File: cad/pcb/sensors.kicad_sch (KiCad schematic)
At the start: 7 parts, among them IC4 MXC4005XC, IC5 KTS1620ERG-TR, Q2 1541201NEA400

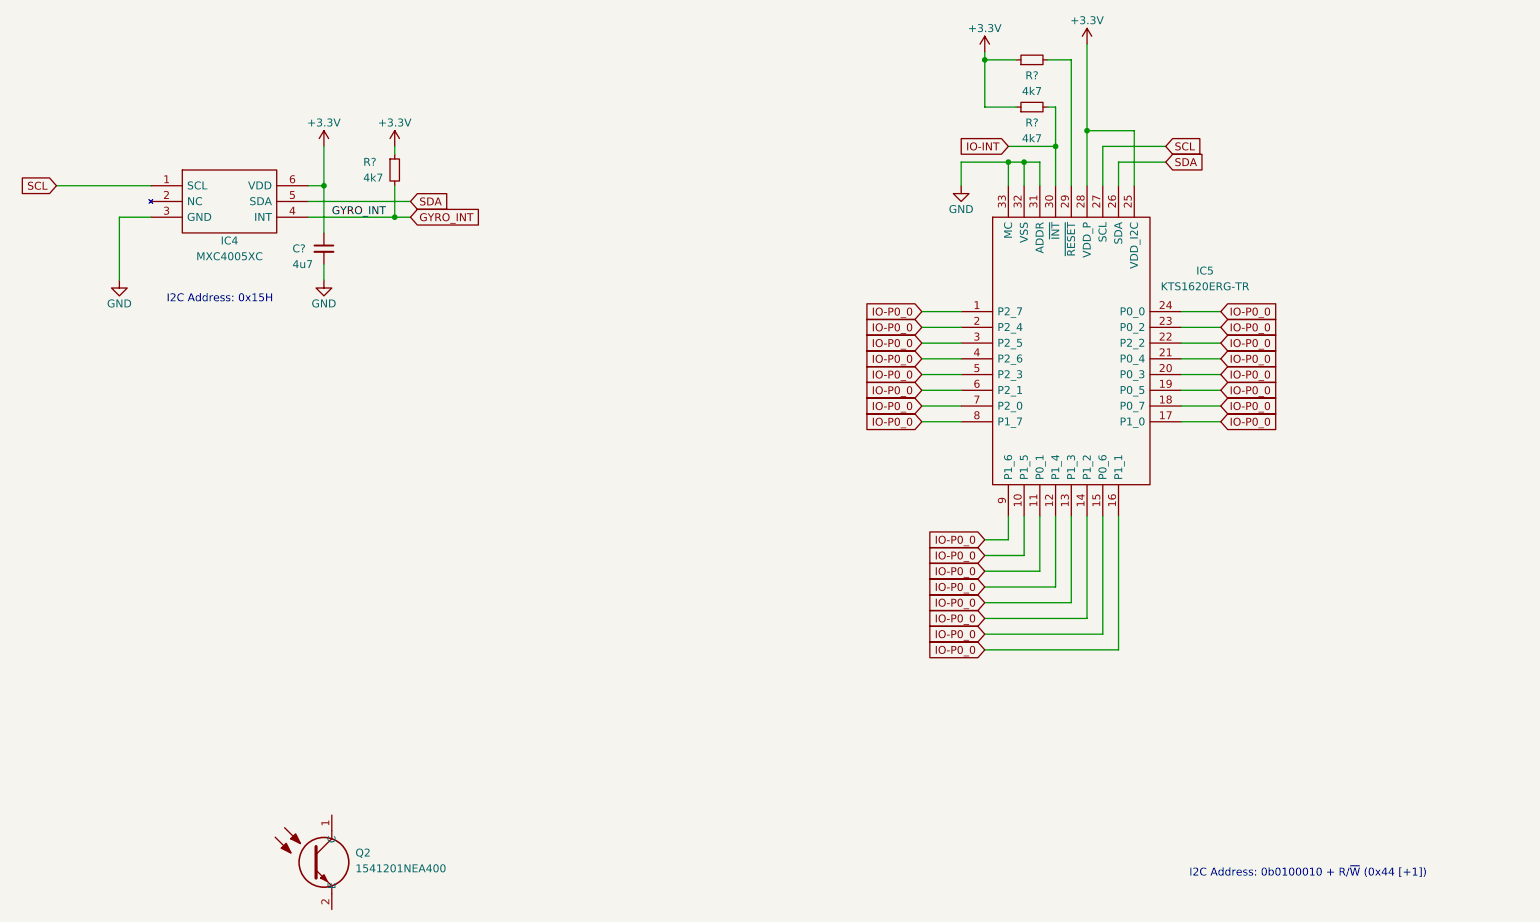
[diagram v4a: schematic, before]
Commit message: add LEDs for LED ring
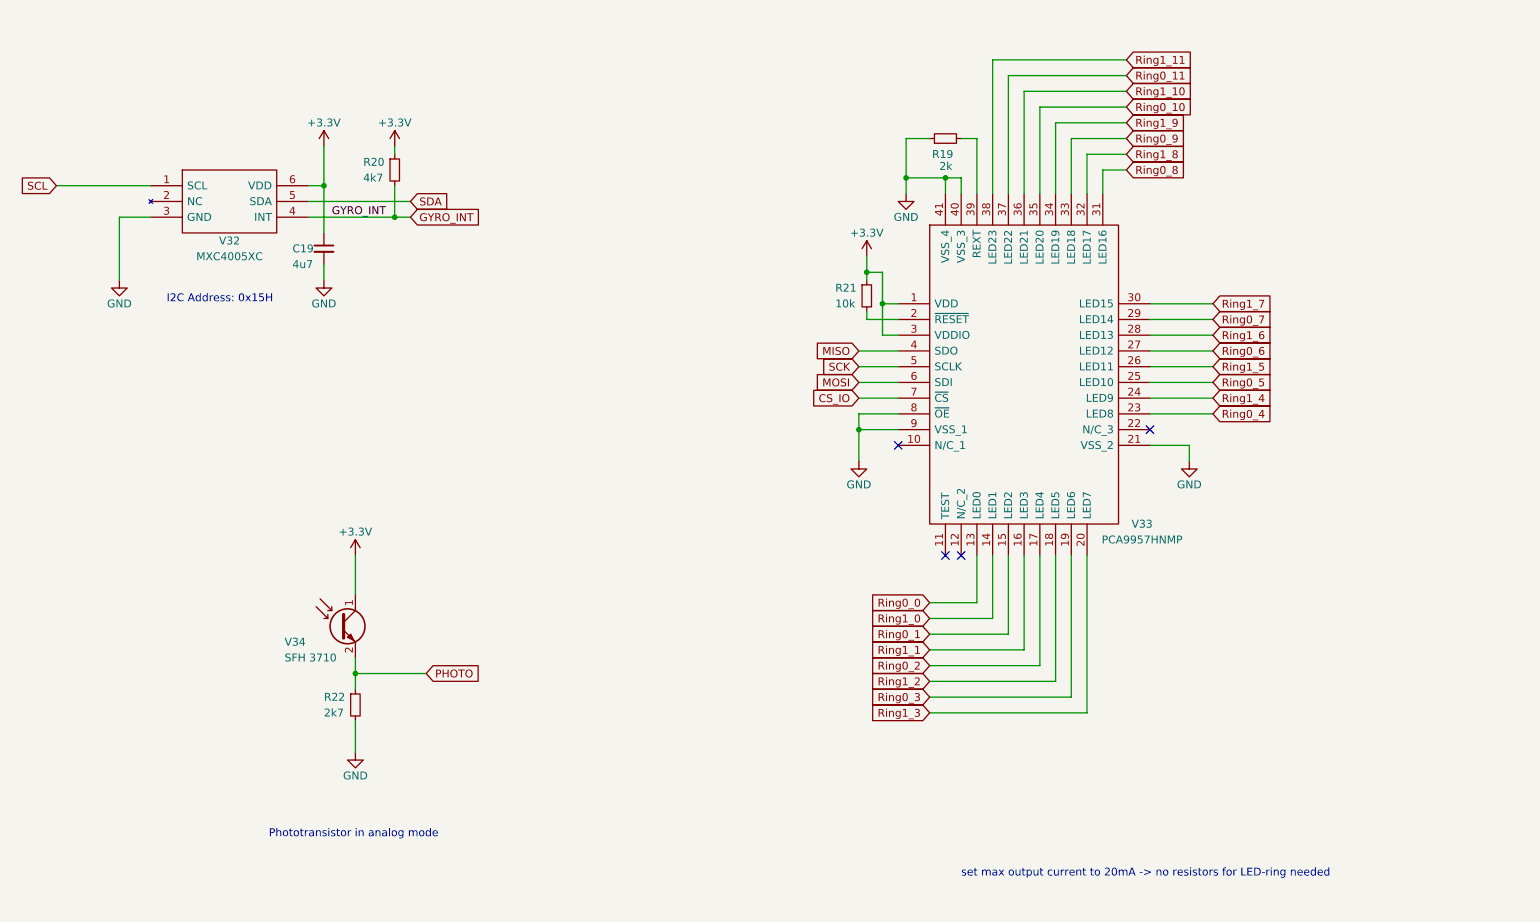
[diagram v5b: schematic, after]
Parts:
- removed IC5: KTS1620ERG-TR, QFN50P500X500X80-33N-D, symbol I/O-Expander:KTS1620ERG-TR
- removed Q2: 1541201NEA400, 1541201NEA400, symbol Phototransistor:1541201NEA400
- removed R? (x2): 4k7, symbol Device:R_Small
- added R19: 2k, symbol Device:R_Small
- added R21: 10k, symbol Device:R_Small
- added R22: 2k7, symbol Device:R_Small
- added V33: PCA9957HNMP, IO Expander:PCA9957HNMP, symbol I/O-Expander:PCA9957HNMP
- added V34: SFH 3710, symbol Device:Q_Photo_NPN
- V32: renamed from IC4; footprint MXC4005XC -> Gyroscope:MXC4005XC
- gave numbers to parts that had none: 2
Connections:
- net +3.3V: now also R21.1, V33.1 (VDD), V33.3 (VDDIO), V34.1 (C)
- net GND: now also R19.1, R22.2, V33.21 (VSS_2), V33.40 (VSS_3), V33.41 (VSS_4), V33.8 (~{OE}), V33.9 (VSS_1)
- new net: R21.2, V33.2 (~{RESET})
- new net: R19.2, V33.39 (REXT)
- new net CS_IO: V33.7 (~{CS})
- new net MISO: V33.4 (SDO)
- new net MOSI: V33.6 (SDI)
- new net PHOTO: R22.1, V34.2 (E)
- new net Ring0_0: V33.13 (LED0)
- new net Ring0_1: V33.15 (LED2)
- new net Ring0_10: V33.35 (LED20)
- new net Ring0_11: V33.37 (LED22)
- new net Ring0_2: V33.17 (LED4)
- new net Ring0_3: V33.19 (LED6)
- new net Ring0_4: V33.23 (LED8)
- new net Ring0_5: V33.25 (LED10)
- new net Ring0_6: V33.27 (LED12)
- new net Ring0_7: V33.29 (LED14)
- new net Ring0_8: V33.31 (LED16)
- new net Ring0_9: V33.33 (LED18)
- new net Ring1_0: V33.14 (LED1)
- new net Ring1_1: V33.16 (LED3)
- new net Ring1_10: V33.36 (LED21)
- new net Ring1_11: V33.38 (LED23)
- new net Ring1_2: V33.18 (LED5)
- new net Ring1_3: V33.20 (LED7)
- new net Ring1_4: V33.24 (LED9)
- new net Ring1_5: V33.26 (LED11)
- new net Ring1_6: V33.28 (LED13)
- new net Ring1_7: V33.30 (LED15)
- new net Ring1_8: V33.32 (LED17)
- new net Ring1_9: V33.34 (LED19)
- new net SCK: V33.5 (SCLK)
- no-connect marks 0 -> 4
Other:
- note added: "Phototransistor in analog mode"
- note added: "set max output current to 20mA -> no resistors for LED-ring needed"
- note removed: "I2C Address: 0b0100010 + R/~{W} (0x44 [+1])"

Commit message: add testpoints & connectors
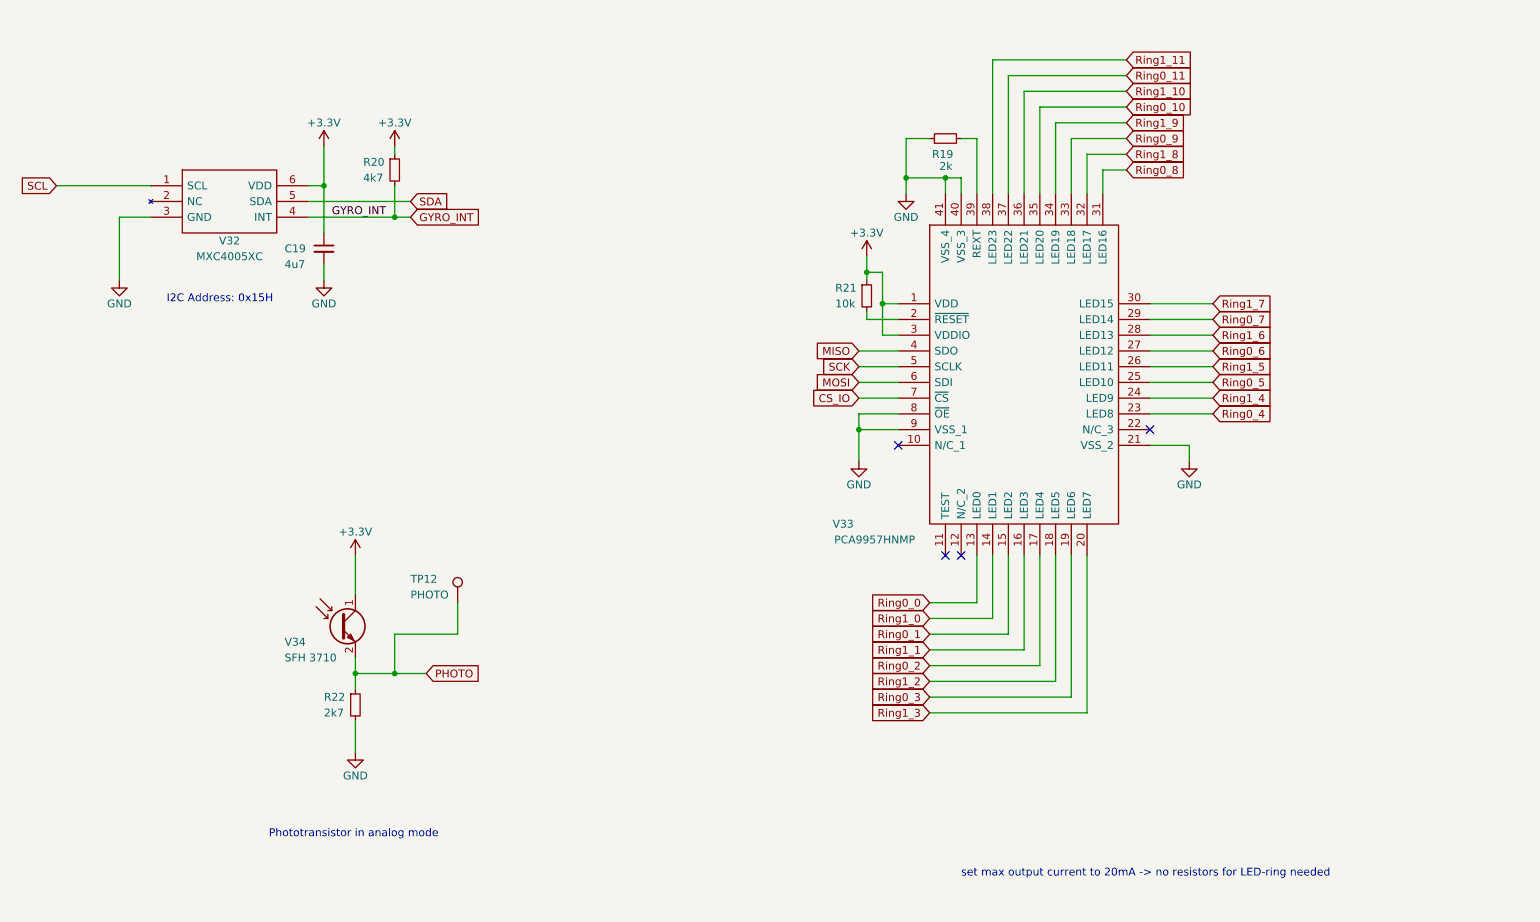
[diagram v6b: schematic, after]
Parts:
- added TP12: PHOTO, symbol Connector:TestPoint
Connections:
- net PHOTO: now also TP12.1
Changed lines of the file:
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@@
   (junction (at 168.91 91.44) (diameter 0) (color 0 0 0 0)
+  )
+  (junction (at 93.98 130.81) (diameter 0) (color 0 0 0 0)
   )
   (junction (at 93.98 57.15) (diameter 0) (color 0 0 0 0)
@@
     (stroke (width 0) (type default) (color 0 0 0 0))
   )
-  (wire (pts (xy 99.06 130.81) (xy 87.63 130.81))
+  (wire (pts (xy 99.06 130.81) (xy 93.98 130.81))
     (stroke (width 0) (type default) (color 0 0 0 0))
   )
@@
     (stroke (width 0) (type default) (color 0 0 0 0))
   )
+  (wire (pts (xy 93.98 124.46) (xy 93.98 130.81))
+    (stroke (width 0) (type default) (color 0 0 0 0))
+  )
   (wire (pts (xy 200.66 111.76) (xy 200.66 132.08))
     (stroke (width 0) (type default) (color 0 0 0 0))
@@
     (stroke (width 0) (type default) (color 0 0 0 0))
   )
+  (wire (pts (xy 104.14 119.38) (xy 104.14 124.46))
+    (stroke (width 0) (type default) (color 0 0 0 0))
+  )
   (wire (pts (xy 80.01 54.61) (xy 96.52 54.61))
     (stroke (width 0) (type default) (color 0 0 0 0))
@@
     (stroke (width 0) (type default) (color 0 0 0 0))
   )
+  (wire (pts (xy 93.98 130.81) (xy 87.63 130.81))
+    (stroke (width 0) (type default) (color 0 0 0 0))
+  )
   (wire (pts (xy 215.9 71.12) (xy 226.06 71.12))
     (stroke (width 0) (type default) (color 0 0 0 0))
@@
   )
   (wire (pts (xy 87.63 143.51) (xy 87.63 138.43))
+    (stroke (width 0) (type default) (color 0 0 0 0))
+  )
+  (wire (pts (xy 104.14 124.46) (xy 93.98 124.46))
     (stroke (width 0) (type default) (color 0 0 0 0))
   )
@@
   (symbol (lib_id "power:+3.3V") (at 82.55 45.72 0) (unit 1)
     (in_bom yes) (on_board yes)
-    (property "Reference" "#PWR063" (id 0) (at 82.55 49.53 0)
+    (property "Reference" "#PWR066" (id 0) (at 82.55 49.53 0)
       (effects (font (size 1.27 1.27)) hide)
     )
@@
   (symbol (lib_id "power:GND") (at 49.53 67.31 0) (unit 1)
     (in_bom yes) (on_board yes)
-    (property "Reference" "#PWR067" (id 0) (at 49.53 73.66 0)
+    (property "Reference" "#PWR070" (id 0) (at 49.53 73.66 0)
       (effects (font (size 1.27 1.27)) hide)
     )
@@
   (symbol (lib_id "power:+3.3V") (at 170.18 63.5 0) (unit 1)
     (in_bom yes) (on_board yes)
-    (property "Reference" "#PWR066" (id 0) (at 170.18 67.31 0)
+    (property "Reference" "#PWR069" (id 0) (at 170.18 67.31 0)
       (effects (font (size 1.27 1.27)) hide)
     )
@@
   (symbol (lib_id "power:GND") (at 87.63 143.51 0) (unit 1)
     (in_bom yes) (on_board yes)
-    (property "Reference" "#PWR072" (id 0) (at 87.63 149.86 0)
+    (property "Reference" "#PWR075" (id 0) (at 87.63 149.86 0)
       (effects (font (size 1.27 1.27)) hide)
     )
@@
   (symbol (lib_id "power:GND") (at 176.53 53.34 0) (unit 1)
     (in_bom yes) (on_board yes)
-    (property "Reference" "#PWR065" (id 0) (at 176.53 59.69 0)
+    (property "Reference" "#PWR068" (id 0) (at 176.53 59.69 0)
       (effects (font (size 1.27 1.27)) hide)
     )
@@
   (symbol (lib_id "power:GND") (at 82.55 67.31 0) (unit 1)
     (in_bom yes) (on_board yes)
-    (property "Reference" "#PWR068" (id 0) (at 82.55 73.66 0)
+    (property "Reference" "#PWR071" (id 0) (at 82.55 73.66 0)
       (effects (font (size 1.27 1.27)) hide)
     )
@@
   (symbol (lib_id "power:GND") (at 168.91 96.52 0) (unit 1)
     (in_bom yes) (on_board yes)
-    (property "Reference" "#PWR069" (id 0) (at 168.91 102.87 0)
+    (property "Reference" "#PWR072" (id 0) (at 168.91 102.87 0)
       (effects (font (size 1.27 1.27)) hide)
     )
@@
   (symbol (lib_id "Device:C_Small") (at 82.55 62.23 0) (unit 1)
     (in_bom yes) (on_board yes)
-    (property "Reference" "C19" (id 0) (at 77.47 62.23 0)
-      (effects (font (size 1.27 1.27)) (justify left))
-    )
-    (property "Value" "4u7" (id 1) (at 77.47 64.77 0)
+    (property "Reference" "C19" (id 0) (at 76.2 62.23 0)
+      (effects (font (size 1.27 1.27)) (justify left))
+    )
+    (property "Value" "4u7" (id 1) (at 76.2 64.77 0)
       (effects (font (size 1.27 1.27)) (justify left))
     )
@@
   (symbol (lib_id "I{slash}O-Expander:PCA9957HNMP") (at 175.26 71.12 0) (unit 1)
     (in_bom yes) (on_board yes)
-    (property "Reference" "V33" (id 0) (at 214.63 106.68 0))
-    (property "Value" "PCA9957HNMP" (id 1) (at 214.63 109.22 0))
+    (property "Reference" "V33" (id 0) (at 166.37 106.68 0))
+    (property "Value" "PCA9957HNMP" (id 1) (at 171.45 109.22 0))
     (property "Footprint" "IO Expander:PCA9957HNMP" (id 2) (at 212.09 58.42 0)
       (effects (font (size 1.27 1.27)) (justify left) hide)
@@
   (symbol (lib_id "power:GND") (at 222.25 96.52 0) (unit 1)
     (in_bom yes) (on_board yes)
-    (property "Reference" "#PWR070" (id 0) (at 222.25 102.87 0)
+    (property "Reference" "#PWR073" (id 0) (at 222.25 102.87 0)
       (effects (font (size 1.27 1.27)) hide)
     )
@@
     (pin "1")
   )
+  (symbol (lib_id "Connector:TestPoint") (at 104.14 119.38 0) (unit 1)
+    (in_bom yes) (on_board yes)
+    (property "Reference" "TP12" (id 0) (at 96.52 115.57 0)
+      (effects (font (size 1.27 1.27)) (justify left))
+    )
+    (property "Value" "PHOTO" (id 1) (at 96.52 118.11 0)
+      (effects (font (size 1.27 1.27)) (justify left))
+    )
+    (property "Footprint" "" (id 2) (at 109.22 119.38 0)
+      (effects (font (size 1.27 1.27)) hide)
+    )
+    (property "Datasheet" "~" (id 3) (at 109.22 119.38 0)
+      (effects (font (size 1.27 1.27)) hide)
+    )
+    (pin "1")
+  )
   (symbol (lib_id "power:+3.3V") (at 93.98 45.72 0) (unit 1)
     (in_bom yes) (on_board yes)
-    (property "Reference" "#PWR064" (id 0) (at 93.98 49.53 0)
+    (property "Reference" "#PWR067" (id 0) (at 93.98 49.53 0)
       (effects (font (size 1.27 1.27)) hide)
     )
@@
   (symbol (lib_id "power:+3.3V") (at 87.63 111.76 0) (unit 1)
     (in_bom yes) (on_board yes)
-    (property "Reference" "#PWR071" (id 0) (at 87.63 115.57 0)
-      (effects (font (size 1.27 1.27)) hide)
-    )
+    (property "Reference" "#PWR074" (id 0) (at 87.63 115.57 0)
+      (effects (font (size 1.27 1.27)) hide)
+    )

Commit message: add usb-c footprint
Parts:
- renumbered R19 to R22, R20 to R23, R21 to R24, R22 to R25
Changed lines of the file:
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@@
   (symbol (lib_id "power:+3.3V") (at 82.55 45.72 0) (unit 1)
     (in_bom yes) (on_board yes)
-    (property "Reference" "#PWR066" (id 0) (at 82.55 49.53 0)
+    (property "Reference" "#PWR072" (id 0) (at 82.55 49.53 0)
       (effects (font (size 1.27 1.27)) hide)
     )
@@
   (symbol (lib_id "power:GND") (at 49.53 67.31 0) (unit 1)
     (in_bom yes) (on_board yes)
-    (property "Reference" "#PWR070" (id 0) (at 49.53 73.66 0)
+    (property "Reference" "#PWR076" (id 0) (at 49.53 73.66 0)
       (effects (font (size 1.27 1.27)) hide)
     )
@@
   (symbol (lib_id "Device:R_Small") (at 170.18 69.85 0) (unit 1)
     (in_bom yes) (on_board yes)
-    (property "Reference" "R21" (id 0) (at 165.1 68.58 0)
+    (property "Reference" "R24" (id 0) (at 165.1 68.58 0)
       (effects (font (size 1.27 1.27)) (justify left))
     )
@@
   (symbol (lib_id "power:+3.3V") (at 170.18 63.5 0) (unit 1)
     (in_bom yes) (on_board yes)
-    (property "Reference" "#PWR069" (id 0) (at 170.18 67.31 0)
+    (property "Reference" "#PWR075" (id 0) (at 170.18 67.31 0)
       (effects (font (size 1.27 1.27)) hide)
     )
@@
   (symbol (lib_id "power:GND") (at 87.63 143.51 0) (unit 1)
     (in_bom yes) (on_board yes)
-    (property "Reference" "#PWR075" (id 0) (at 87.63 149.86 0)
+    (property "Reference" "#PWR081" (id 0) (at 87.63 149.86 0)
       (effects (font (size 1.27 1.27)) hide)
     )
@@
   (symbol (lib_id "Device:R_Small") (at 93.98 49.53 0) (unit 1)
     (in_bom yes) (on_board yes)
-    (property "Reference" "R20" (id 0) (at 88.9 48.26 0)
+    (property "Reference" "R23" (id 0) (at 88.9 48.26 0)
       (effects (font (size 1.27 1.27)) (justify left))
     )
@@
   (symbol (lib_id "Device:R_Small") (at 182.88 44.45 90) (unit 1)
     (in_bom yes) (on_board yes)
-    (property "Reference" "R19" (id 0) (at 184.15 46.99 90)
+    (property "Reference" "R22" (id 0) (at 184.15 46.99 90)
       (effects (font (size 1.27 1.27)) (justify left))
     )
@@
   (symbol (lib_id "power:GND") (at 176.53 53.34 0) (unit 1)
     (in_bom yes) (on_board yes)
-    (property "Reference" "#PWR068" (id 0) (at 176.53 59.69 0)
+    (property "Reference" "#PWR074" (id 0) (at 176.53 59.69 0)
       (effects (font (size 1.27 1.27)) hide)
     )
@@
   (symbol (lib_id "power:GND") (at 82.55 67.31 0) (unit 1)
     (in_bom yes) (on_board yes)
-    (property "Reference" "#PWR071" (id 0) (at 82.55 73.66 0)
+    (property "Reference" "#PWR077" (id 0) (at 82.55 73.66 0)
       (effects (font (size 1.27 1.27)) hide)
     )
@@
   (symbol (lib_id "power:GND") (at 168.91 96.52 0) (unit 1)
     (in_bom yes) (on_board yes)
-    (property "Reference" "#PWR072" (id 0) (at 168.91 102.87 0)
+    (property "Reference" "#PWR078" (id 0) (at 168.91 102.87 0)
       (effects (font (size 1.27 1.27)) hide)
     )
@@
   (symbol (lib_id "Device:R_Small") (at 87.63 135.89 0) (unit 1)
     (in_bom yes) (on_board yes)
-    (property "Reference" "R22" (id 0) (at 82.55 134.62 0)
+    (property "Reference" "R25" (id 0) (at 82.55 134.62 0)
       (effects (font (size 1.27 1.27)) (justify left))
     )
@@
   (symbol (lib_id "power:GND") (at 222.25 96.52 0) (unit 1)
     (in_bom yes) (on_board yes)
-    (property "Reference" "#PWR073" (id 0) (at 222.25 102.87 0)
+    (property "Reference" "#PWR079" (id 0) (at 222.25 102.87 0)
       (effects (font (size 1.27 1.27)) hide)
     )
@@
   (symbol (lib_id "power:+3.3V") (at 93.98 45.72 0) (unit 1)
     (in_bom yes) (on_board yes)
-    (property "Reference" "#PWR067" (id 0) (at 93.98 49.53 0)
+    (property "Reference" "#PWR073" (id 0) (at 93.98 49.53 0)
       (effects (font (size 1.27 1.27)) hide)
     )
@@
   (symbol (lib_id "power:+3.3V") (at 87.63 111.76 0) (unit 1)
     (in_bom yes) (on_board yes)
-    (property "Reference" "#PWR074" (id 0) (at 87.63 115.57 0)
-      (effects (font (size 1.27 1.27)) hide)
-    )
+    (property "Reference" "#PWR080" (id 0) (at 87.63 115.57 0)
+      (effects (font (size 1.27 1.27)) hide)
+    )
